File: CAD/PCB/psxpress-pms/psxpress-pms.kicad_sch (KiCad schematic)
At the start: 40 parts, among them IC1 BQ25606RGER, IC2 MAX16054AZT+T, IC3 TPS61023DRLT, IC4 TPS564255DRLR, Q1 AO3401A, SW1 SW_SPST

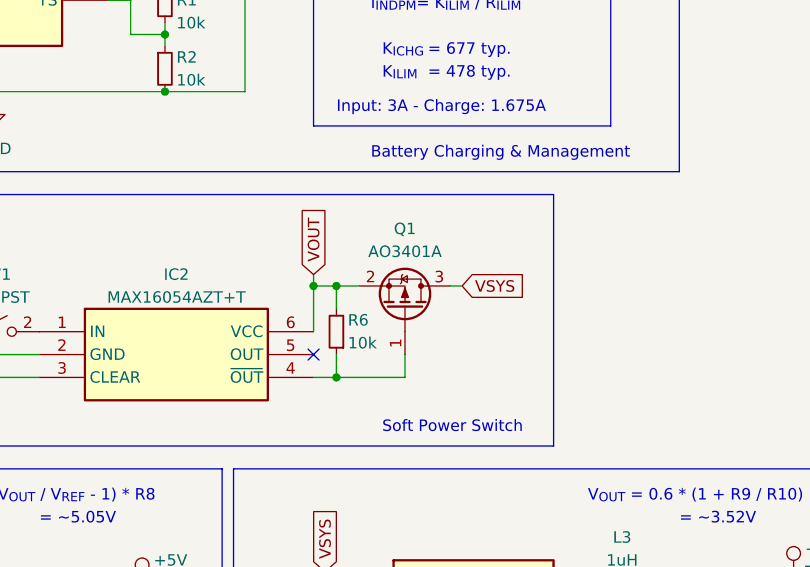
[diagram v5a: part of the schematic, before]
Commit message: pms - switch soft power mosfet to AONR21117 - schematic finished
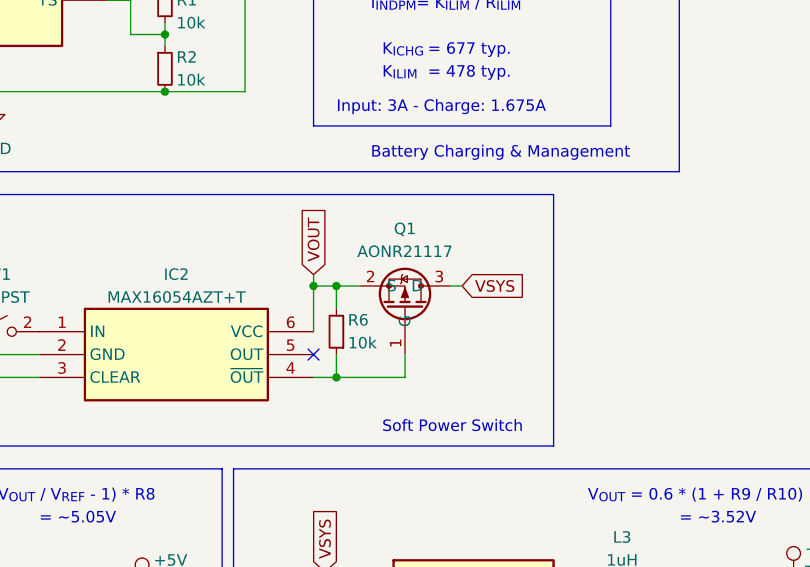
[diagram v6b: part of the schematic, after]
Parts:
- removed Q1: AO3401A, Package_TO_SOT_SMD:SOT-23, symbol Transistor_FET:AO3401A
- added Q1: AONR21117, symbol AONR21117:AONR21117
- C1, C10, C11, C12, C13, C14, C2, C3, C4, C5, C6, C7, C8, C9: footprint (none) -> Capacitor_SMD:C_0603_1608Metric
- IC1: footprint QFN50P400X400X100-25N-D -> BQ25606RGER:QFN50P400X400X100-25N-D
- IC2: footprint SOT95P275X110-6N -> MAX16054AZT+T:SOT95P275X110-6N
- IC3, IC4: footprint SOTFL50P160X60-6N -> Package_TO_SOT_SMD:SOT-666
- R1, R10, R2, R3, R4, R5, R6, R7, R8, R9: footprint (none) -> Resistor_SMD:R_0603_1608Metric
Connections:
- net VOUT: now also Q1.2 (S)
- net VSYS: now also Q1.3 (D)
- net at IC2.4 (~{OUT}), R6.1: now also Q1.1 (G)
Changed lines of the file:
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@@
-    )
-  )
-  (symbol (lib_id "Transistor_FET:AO3401A") (at 167.64 102.87 270) (mirror x) (unit 1)
-    (in_bom yes) (on_board yes) (dnp no)
-    (property "Reference" "Q1" (at 167.64 93.98 90)
-      (effects (font (size 1.27 1.27)))
-    )
-    (property "Value" "AO3401A" (at 167.64 96.52 90)
-      (effects (font (size 1.27 1.27)))
-    )
-    (property "Footprint" "Package_TO_SOT_SMD:SOT-23" (at 165.735 97.79 0)
-      (effects (font (size 1.27 1.27) italic) (justify left) hide)
-    )
-    (property "Datasheet" "http://www.aosmd.com/pdfs/datasheet/AO3401A.pdf" (at 167.64 102.87 0)
-      (effects (font (size 1.27 1.27)) (justify left) hide)
-    )
-    (pin "1")
-    (pin "2")
-    (pin "3")
-    (instances
-      (project "psxpress-pms"
-        (path "/b46ebcbe-5ef3-41ff-bf92-95c75415e5a2"
-          (reference "Q1") (unit 1)
-        )
-      )
     )
   )
@@
       (effects (font (size 1.27 1.27)) (justify right))
     )
-    (property "Footprint" "" (at 203.2 140.97 0)
+    (property "Footprint" "Capacitor_SMD:C_0603_1608Metric" (at 203.2 140.97 0)
       (effects (font (size 1.27 1.27)) hide)
     )
@@
       (effects (font (size 1.27 1.27)))
     )
-    (property "Footprint" "" (at 180.34 30.48 0)
+    (property "Footprint" "Resistor_SMD:R_0603_1608Metric" (at 180.34 30.48 0)
       (effects (font (size 1.27 1.27)) hide)
     )
@@
       (effects (font (size 1.27 1.27)) (justify left))
     )
-    (property "Footprint" "" (at 157.48 43.18 0)
+    (property "Footprint" "Capacitor_SMD:C_0603_1608Metric" (at 157.48 43.18 0)
       (effects (font (size 1.27 1.27)) hide)
     )
@@
       (effects (font (size 1.27 1.27)) (justify right))
     )
-    (property "Footprint" "" (at 130.81 140.97 0)
+    (property "Footprint" "Capacitor_SMD:C_0603_1608Metric" (at 130.81 140.97 0)
       (effects (font (size 1.27 1.27)) hide)
     )
@@
       (effects (font (size 1.27 1.27)) (justify left))
     )
-    (property "Footprint" "" (at 121.92 138.43 0)
+    (property "Footprint" "Resistor_SMD:R_0603_1608Metric" (at 121.92 138.43 0)
       (effects (font (size 1.27 1.27)) hide)
     )
@@
       (effects (font (size 1.27 1.27)) (justify left))
     )
-    (property "Footprint" "" (at 146.05 66.04 0)
+    (property "Footprint" "Capacitor_SMD:C_0603_1608Metric" (at 146.05 66.04 0)
       (effects (font (size 1.27 1.27)) hide)
     )
@@
       (effects (font (size 1.27 1.27)))
     )
-    (property "Footprint" "" (at 105.41 60.96 0)
+    (property "Footprint" "Resistor_SMD:R_0603_1608Metric" (at 105.41 60.96 0)
       (effects (font (size 1.27 1.27)) hide)
     )
@@
       (effects (font (size 1.27 1.27)) (justify left))
     )
-    (property "Footprint" "" (at 140.97 76.2 0)
+    (property "Footprint" "Resistor_SMD:R_0603_1608Metric" (at 140.97 76.2 0)
       (effects (font (size 1.27 1.27)) hide)
     )
@@
       (effects (font (size 1.27 1.27)))
     )
-    (property "Footprint" "" (at 105.41 48.26 0)
+    (property "Footprint" "Resistor_SMD:R_0603_1608Metric" (at 105.41 48.26 0)
       (effects (font (size 1.27 1.27)) hide)
     )
@@
     )
   )
+  (symbol (lib_id "AONR21117:AONR21117") (at 167.64 105.41 270) (mirror x) (unit 1)
+    (in_bom yes) (on_board yes) (dnp no)
+    (property "Reference" "Q1" (at 167.64 93.98 90)
+      (effects (font (size 1.27 1.27)))
+    )
+    (property "Value" "AONR21117" (at 167.64 96.52 90)
+      (effects (font (size 1.27 1.27)))
+    )
+    (property "Footprint" "" (at 172.72 100.33 0)
+      (effects (font (size 1.27 1.27)) hide)
+    )
+    (property "Datasheet" "" (at 172.72 100.33 0)
+      (effects (font (size 1.27 1.27)) hide)
+    )
+    (pin "1")
+    (pin "2")
+    (pin "3")
+    (instances
+      (project "psxpress-pms"
+        (path "/b46ebcbe-5ef3-41ff-bf92-95c75415e5a2"
+          (reference "Q1") (unit 1)
+        )
+      )
+    )
+  )
   (symbol (lib_id "Connector:TestPoint") (at 138.43 134.62 0) (unit 1)
     (in_bom yes) (on_board yes) (dnp no)
@@
       (effects (font (size 1.27 1.27)) (justify left))
     )
-    (property "Footprint" "" (at 146.05 50.8 0)
+    (property "Footprint" "Capacitor_SMD:C_0603_1608Metric" (at 146.05 50.8 0)
       (effects (font (size 1.27 1.27)) hide)
     )
@@
       (effects (font (size 1.27 1.27)) (justify left))
     )
-    (property "Footprint" "" (at 165.1 43.18 0)
+    (property "Footprint" "Capacitor_SMD:C_0603_1608Metric" (at 165.1 43.18 0)
       (effects (font (size 1.27 1.27)) hide)
     )
@@
       (effects (font (size 1.27 1.27)) (justify left))
     )
-    (property "Footprint" "" (at 195.58 137.16 0)
+    (property "Footprint" "Resistor_SMD:R_0603_1608Metric" (at 195.58 137.16 0)
       (effects (font (size 1.27 1.27)) hide)
     )
@@
       (effects (font (size 1.27 1.27)) (justify right))
     )
-    (property "Footprint" "" (at 160.02 105.41 0)
+    (property "Footprint" "Resistor_SMD:R_0603_1608Metric" (at 160.02 105.41 0)
       (effects (font (size 1.27 1.27)) hide)
     )
@@
       (effects (font (size 1.27 1.27)) (justify right))
     )
-    (property "Footprint" "" (at 88.9 137.16 0)
+    (property "Footprint" "Capacitor_SMD:C_0603_1608Metric" (at 88.9 137.16 0)
       (effects (font (size 1.27 1.27)) hide)
     )
@@
       (effects (font (size 1.27 1.27)) (justify right))
     )
-    (property "Footprint" "" (at 138.43 140.97 0)
+    (property "Footprint" "Capacitor_SMD:C_0603_1608Metric" (at 138.43 140.97 0)
       (effects (font (size 1.27 1.27)) hide)
     )
@@
       (effects (font (size 1.27 1.27)) (justify left))
     )
-    (property "Footprint" "" (at 149.86 43.18 0)
+    (property "Footprint" "Capacitor_SMD:C_0603_1608Metric" (at 149.86 43.18 0)
       (effects (font (size 1.27 1.27)) hide)
     )
@@
       (effects (font (size 1.27 1.27)))
     )
-    (property "Footprint" "SOTFL50P160X60-6N" (at 115.57 227 0)
+    (property "Footprint" "Package_TO_SOT_SMD:SOT-666" (at 115.57 227 0)
       (effects (font (size 1.27 1.27)) (justify left top) hide)
     )
@@
       (effects (font (size 1.27 1.27)) (justify left))
     )
-    (property "Footprint" "" (at 195.58 144.78 0)
+    (property "Footprint" "Resistor_SMD:R_0603_1608Metric" (at 195.58 144.78 0)
       (effects (font (size 1.27 1.27)) hide)
     )
@@
       (effects (font (size 1.27 1.27)) (justify left))
     )
-    (property "Footprint" "" (at 140.97 68.58 0)
+    (property "Footprint" "Resistor_SMD:R_0603_1608Metric" (at 140.97 68.58 0)
       (effects (font (size 1.27 1.27)) hide)
     )
@@
       (effects (font (size 1.27 1.27)) (justify right))
     )
-    (property "Footprint" "" (at 210.82 140.97 0)
+    (property "Footprint" "Capacitor_SMD:C_0603_1608Metric" (at 210.82 140.97 0)
       (effects (font (size 1.27 1.27)) hide)
     )
@@
       (effects (font (size 1.27 1.27)) (justify left))
     )
-    (property "Footprint" "" (at 137.16 35.56 0)
+    (property "Footprint" "Capacitor_SMD:C_0603_1608Metric" (at 137.16 35.56 0)
       (effects (font (size 1.27 1.27)) hide)
     )
@@
       (effects (font (size 1.27 1.27)))
     )
-    (property "Footprint" "SOTFL50P160X60-6N" (at 185.42 228.27 0)
+    (property "Footprint" "Package_TO_SOT_SMD:SOT-666" (at 185.42 228.27 0)
       (effects (font (size 1.27 1.27)) (justify left top) hide)
     )
@@
       (effects (font (size 1.27 1.27)))
     )
-    (property "Footprint" "QFN50P400X400X100-25N-D" (at 148.59 139.37 0)
+    (property "Footprint" "BQ25606RGER:QFN50P400X400X100-25N-D" (at 148.59 139.37 0)
       (effects (font (size 1.27 1.27)) (justify left top) hide)
     )
@@
       (effects (font (size 1.27 1.27)) (justify left))
     )
-    (property "Footprint" "" (at 121.92 143.51 0)
+    (property "Footprint" "Resistor_SMD:R_0603_1608Metric" (at 121.92 143.51 0)
       (effects (font (size 1.27 1.27)) hide)
     )
@@
       (effects (font (size 1.27 1.27)) (justify left))
     )
-    (property "Footprint" "" (at 105.41 38.1 0)
+    (property "Footprint" "Capacitor_SMD:C_0603_1608Metric" (at 105.41 38.1 0)
       (effects (font (size 1.27 1.27)) hide)
     )
@@
       (effects (font (size 1.27 1.27)))
     )
-    (property "Footprint" "SOT95P275X110-6N" (at 153.67 200.33 0)
+    (property "Footprint" "MAX16054AZT+T:SOT95P275X110-6N" (at 153.67 200.33 0)
       (effects (font (size 1.27 1.27)) (justify left top) hide)
     )
@@
       (effects (font (size 1.27 1.27)))
     )
-    (property "Footprint" "" (at 135.89 43.18 0)
+    (property "Footprint" "Capacitor_SMD:C_0603_1608Metric" (at 135.89 43.18 0)
       (effects (font (size 1.27 1.27)) hide)
     )
@@
       (effects (font (size 1.27 1.27)) (justify right))
     )
-    (property "Footprint" "" (at 158.75 137.16 0)
-      (effects (font (size 1.27 1.27)) hide)
-    )
+    (property "Footprint" "Capacitor_SMD:C_0603_1608Metric" (at 158.75 137.16 0)
+      (effects (font (size 1.27 1.27)) hide)
+    )

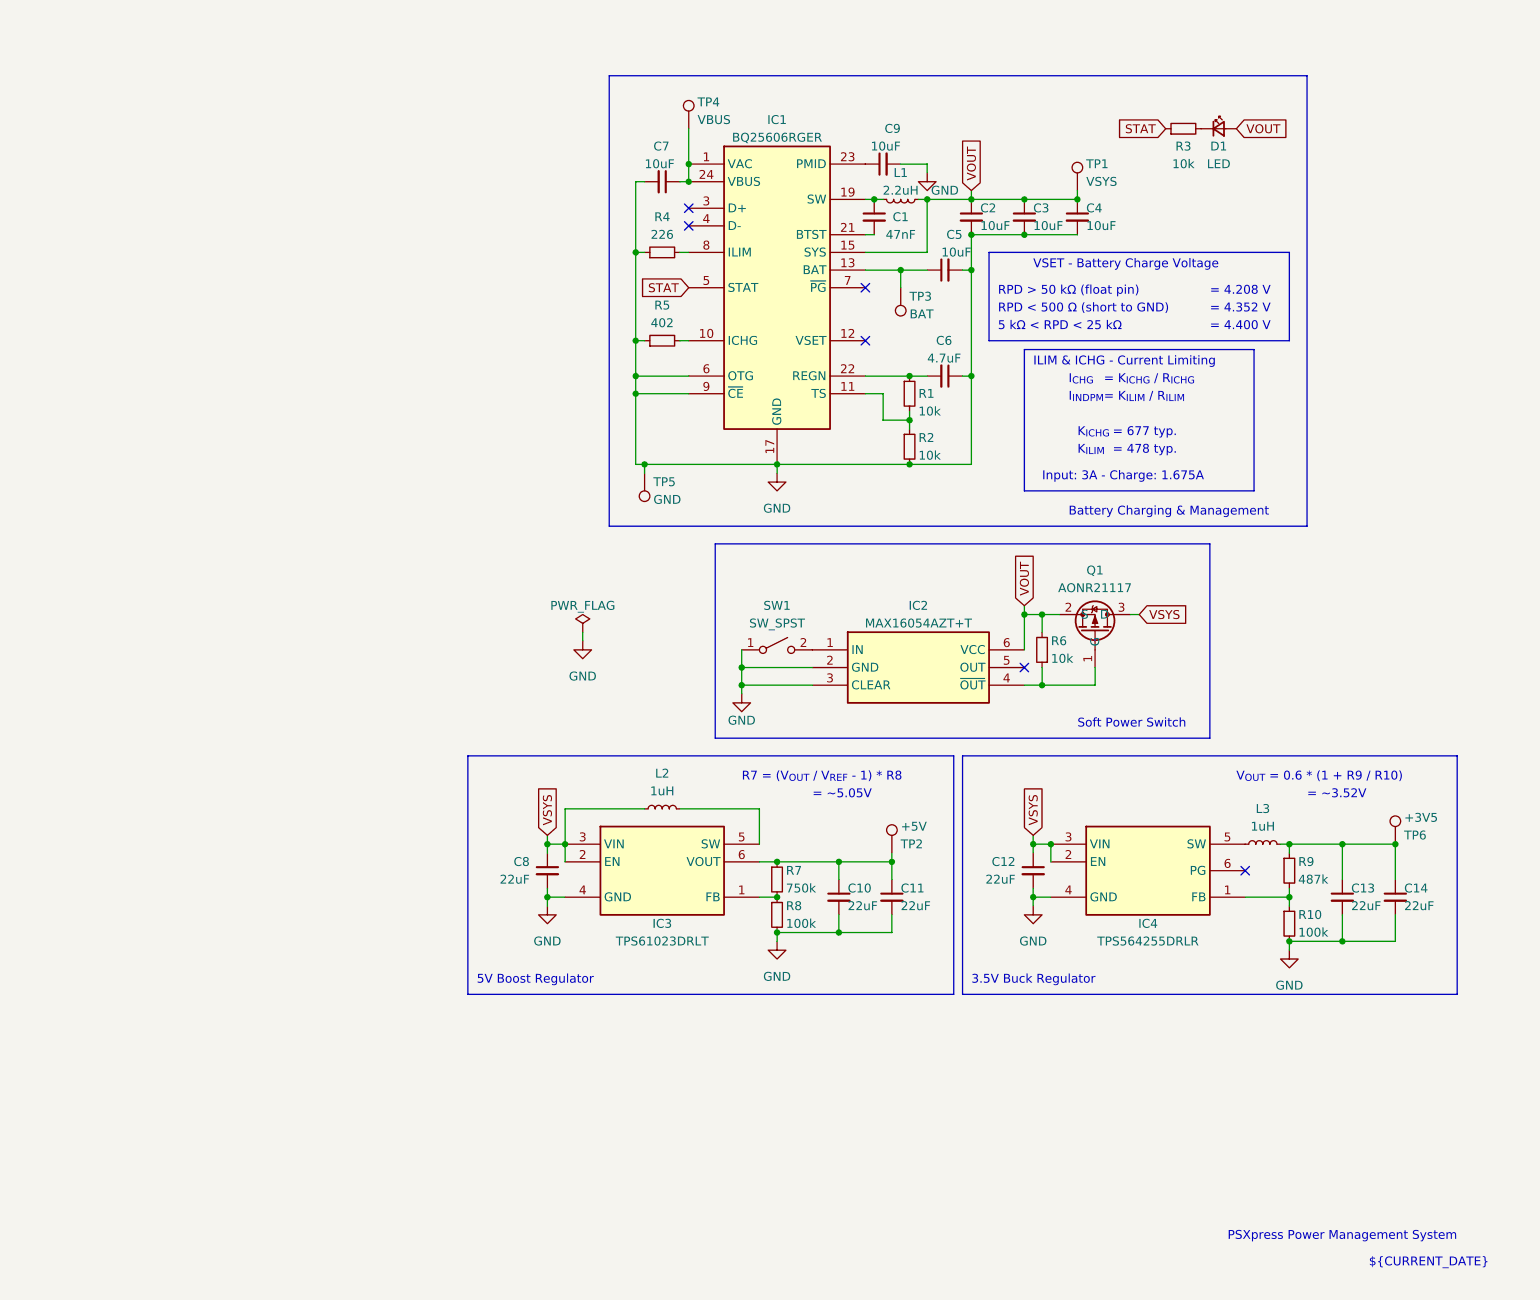
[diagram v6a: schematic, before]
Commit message: pms - update schematic with footprint assignments + add output rail power symbols
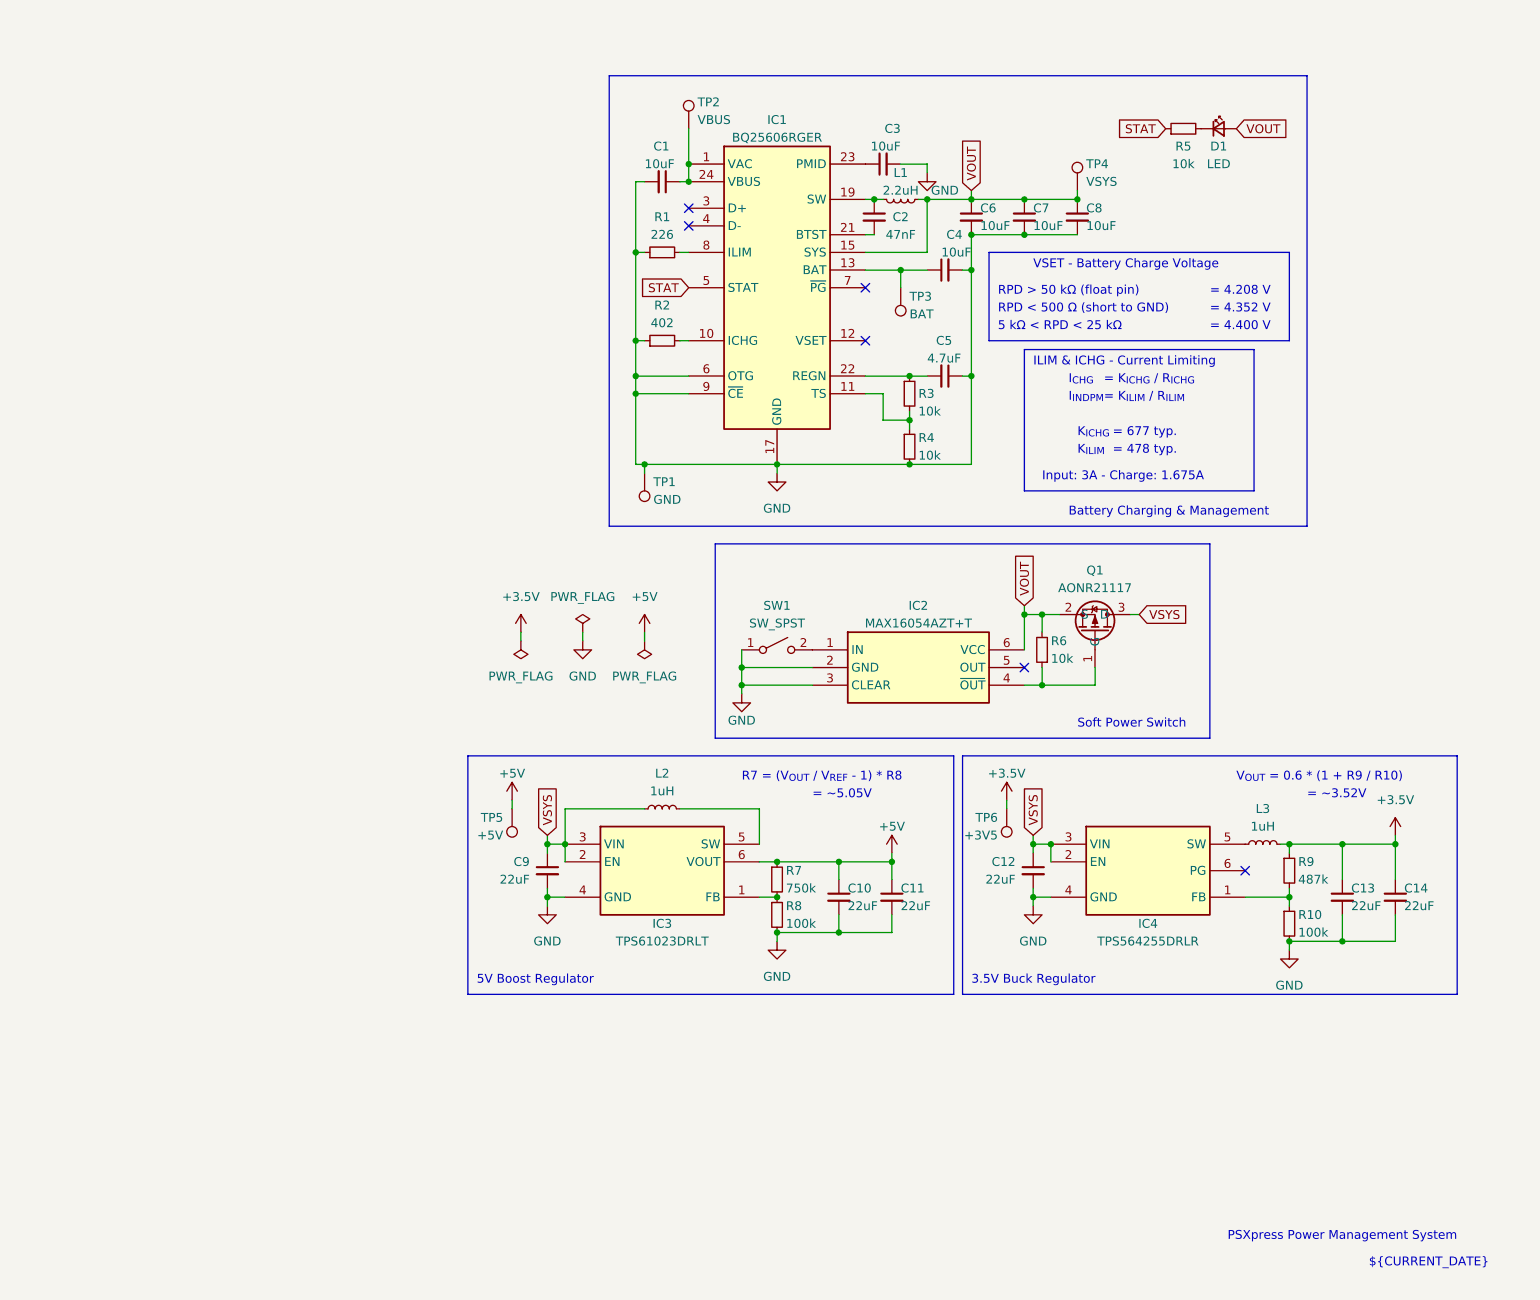
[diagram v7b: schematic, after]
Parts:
- C1: renamed from C7; footprint Capacitor_SMD:C_0603_1608Metric -> Capacitor_SMD:C_0805_2012Metric
- C10, C11, C12, C13, C14: footprint Capacitor_SMD:C_0603_1608Metric -> Capacitor_SMD:C_0805_2012Metric
- C2: renamed from C1; footprint Capacitor_SMD:C_0603_1608Metric -> Capacitor_SMD:C_0805_2012Metric
- C3: renamed from C9; footprint Capacitor_SMD:C_0603_1608Metric -> Capacitor_SMD:C_0805_2012Metric
- C4: renamed from C5; footprint Capacitor_SMD:C_0603_1608Metric -> Capacitor_SMD:C_0805_2012Metric
- C5: renamed from C6; footprint Capacitor_SMD:C_0603_1608Metric -> Capacitor_SMD:C_0805_2012Metric
- C6: renamed from C2; footprint Capacitor_SMD:C_0603_1608Metric -> Capacitor_SMD:C_0805_2012Metric
- C7: renamed from C3; footprint Capacitor_SMD:C_0603_1608Metric -> Capacitor_SMD:C_0805_2012Metric
- C8: renamed from C4; footprint Capacitor_SMD:C_0603_1608Metric -> Capacitor_SMD:C_0805_2012Metric
- C9: renamed from C8; footprint Capacitor_SMD:C_0603_1608Metric -> Capacitor_SMD:C_0805_2012Metric
- L2, L3: footprint (none) -> Inductor_SMD:L_Taiyo-Yuden_MD-4040
- renumbered R4 to R1, R5 to R2, R1 to R3, R2 to R4, R3 to R5, TP5 to TP1, TP4 to TP2, TP1 to TP4, TP2 to TP5
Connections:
- net +3.5V: now reaches C13.1, C14.1, L3.2, R9.1, TP6.1
- net +5V: now reaches C10.1, C11.1, IC3.6 (VOUT), R7.1, TP5.1
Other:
- moved on the sheet: TP5
